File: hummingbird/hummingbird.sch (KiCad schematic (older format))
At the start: 19 parts, among them Y1 Crystal

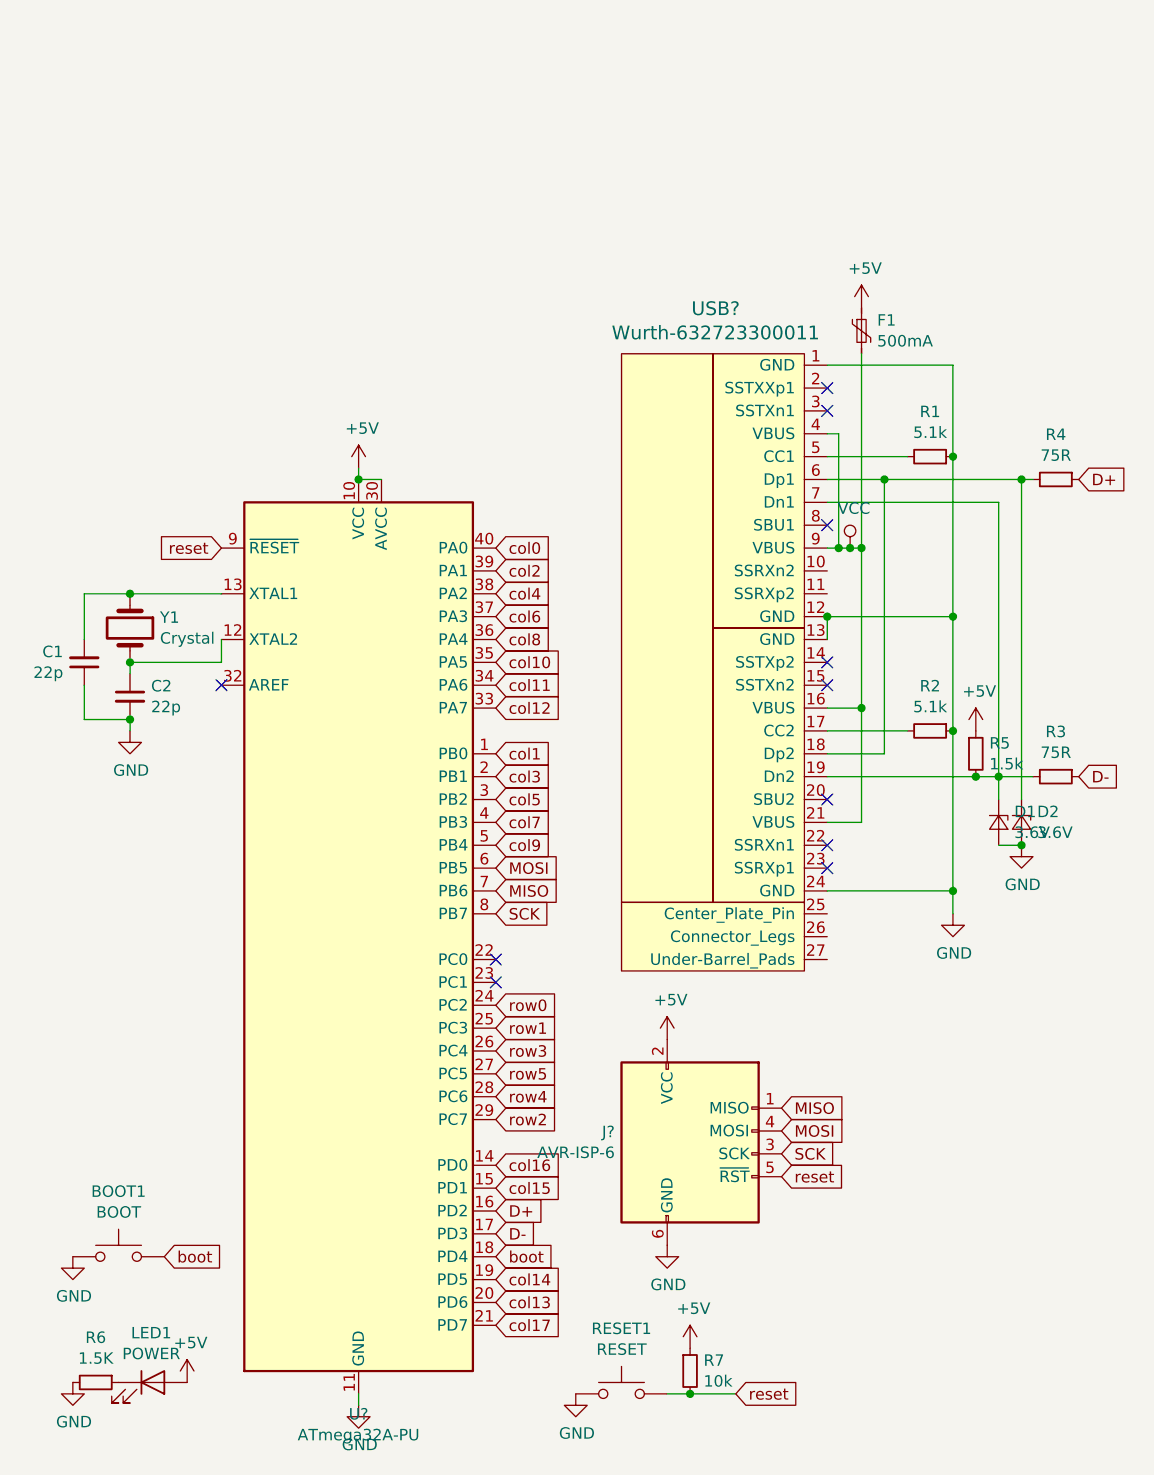
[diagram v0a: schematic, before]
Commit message: use a different mcu
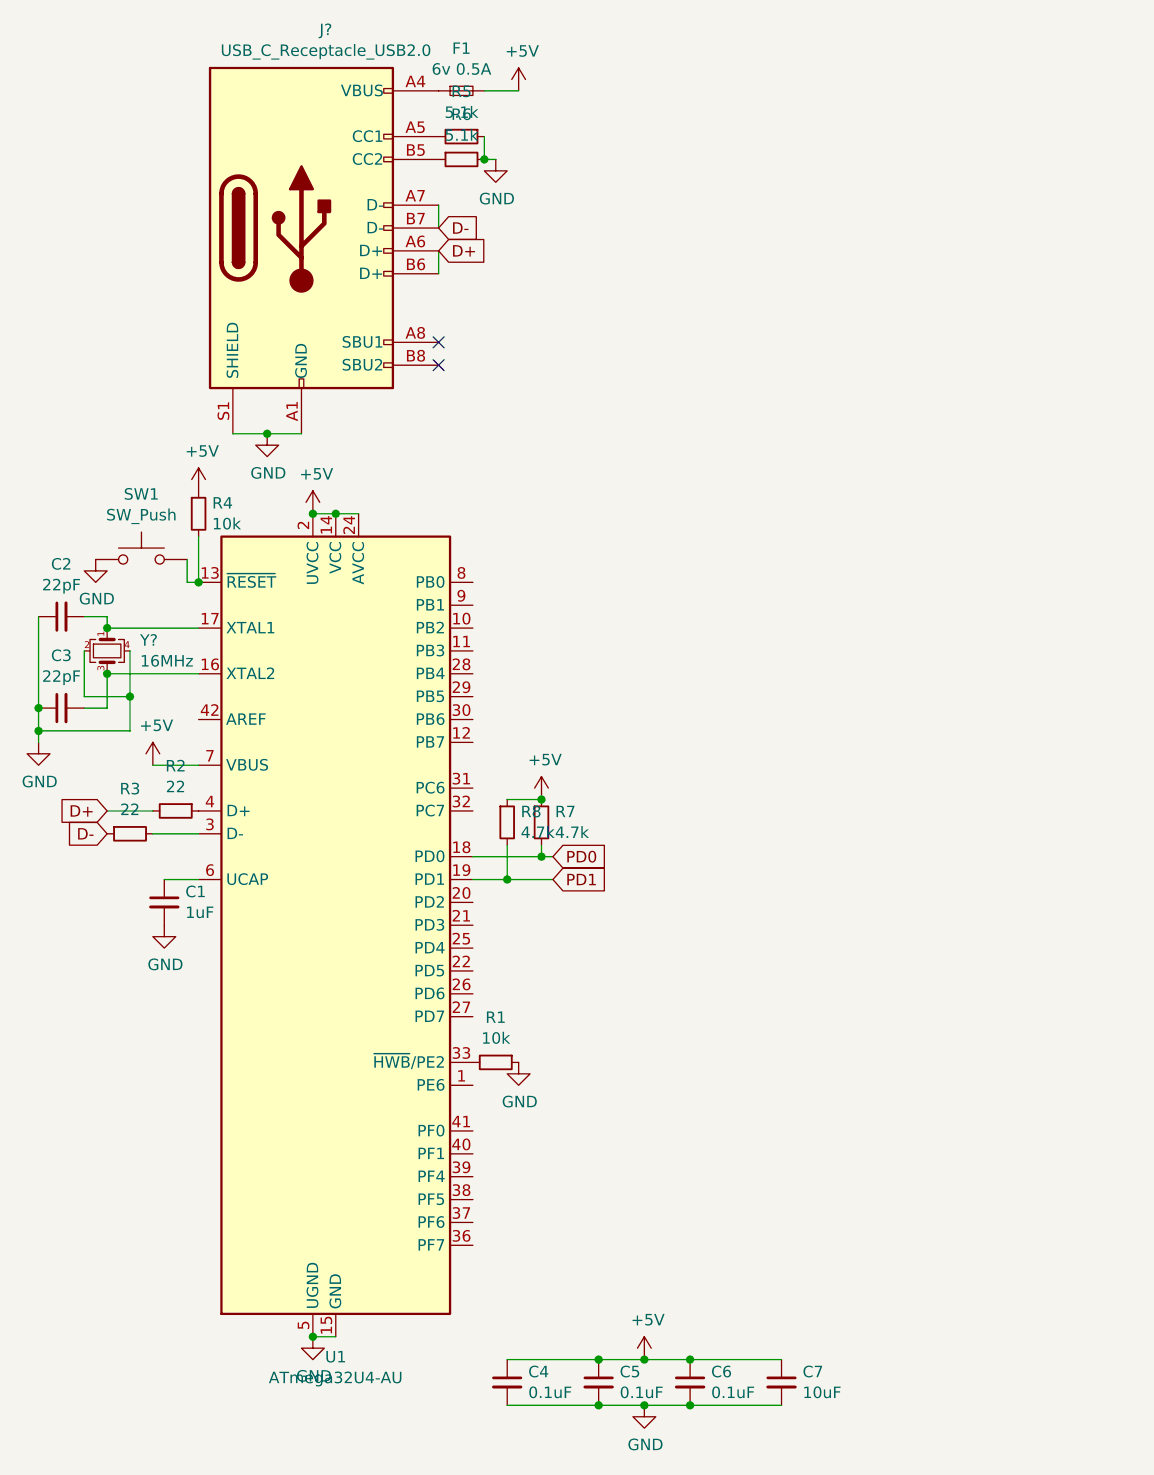
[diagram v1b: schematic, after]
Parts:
- removed BOOT1: BOOT, symbol Switch:SW_Push
- removed D1, D2: 3.6V, symbol Device:D_Zener_Small
- removed F1: 500mA, symbol Device:Polyfuse_Small
- removed J?: AVR-ISP-6, symbol Connector:AVR-ISP-6
- removed LED1: POWER, symbol Device:LED
- removed RESET1: RESET, symbol Switch:SW_Push
- removed U?: ATmega32A-PU, Package_DIP:DIP-40_W15.24mm, symbol MCU_Microchip_ATmega:ATmega32A-PU
- removed USB?: Wurth-632723300011, symbol Type-C:Wurth-632723300011
- removed Y1: Crystal, symbol Device:Crystal
- added C3: 22pF, symbol Device:C_Small
- added C4, C5, C6: 0.1uF, symbol Device:C_Small
- added C7: 10uF, symbol Device:C_Small
- added F1: 6v 0.5A, symbol Device:Fuse_Small
- added J?: USB_C_Receptacle_USB2.0, symbol Connector:USB_C_Receptacle_USB2.0
- added R8: 4.7k, symbol Device:R_Small
- added SW1: SW_Push, symbol Switch:SW_Push
- added U1: ATmega32U4-AU, Package_QFP:TQFP-44_10x10mm_P0.8mm, symbol MCU_Microchip_ATmega:ATmega32U4-AU
- added Y?: 16MHz, symbol Device:Crystal_GND24_Small
- C1: value 22p -> 1uF
- C2: value 22p -> 22pF
- R1: value 5.1k -> 10k
- R2: value 5.1k -> 22
- R3: value 75R -> 22
- R4: value 75R -> 10k
- R5: value 1.5k -> 5.1k
- R6: value 1.5K -> 5.1k
- R7: value 10k -> 4.7k
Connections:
- net +5V: now also R4.1, C4.1, C5.1, C6.1, C7.1, F1.2, R8.1, U1.14 (VCC), U1.2 (UVCC), U1.24 (AVCC), U1.34 (VCC), U1.44 (AVCC), U1.7 (VBUS); no longer R5.1
- net D+: now also R2.2, J?.A6 (D+), J?.B6 (D+); no longer R4.1
- net D-: now also J?.A7 (D-), J?.B7 (D-)
- net GND: now also C1.2, C2.1, R5.1, C3.1, C4.2, C5.2, C6.2, C7.2, J?.A1 (GND), J?.A12 (GND), J?.B1 (GND), J?.B12 (GND), J?.S1 (SHIELD), SW1.1, U1.15 (GND), U1.23 (GND), U1.35 (GND), U1.43 (GND), U1.5 (UGND), Y?.2, Y?.4; no longer C1.1, C2.2, R2.1
- net at R6.1: now also J?.B5 (CC2)
- net at R4.2: now also SW1.2, U1.13 (~RESET)
- net at R3.2: now also U1.3 (D-); no longer R5.2
- net at R1.2: now also U1.33 (~HWB~/PE2)
- net reset renamed PD0
- net PD0: now also U1.18 (PD0)
- new net: C3.2, U1.16 (XTAL2), Y?.3
- new net: C2.2, U1.17 (XTAL1), Y?.1
- new net: R2.1, U1.4 (D+)
- new net: C1.1, U1.6 (UCAP)
- new net: F1.1, J?.A4 (VBUS), J?.A9 (VBUS), J?.B4 (VBUS), J?.B9 (VBUS)
- new net: J?.A5 (CC1), R5.2
- new net PD1: R8.2, U1.19 (PD1)
- no-connect marks 11 -> 2
